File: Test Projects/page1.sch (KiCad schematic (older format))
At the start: 21 parts, among them P1 CONN_01X02, U1 LDO-adj-4term, U2 LDO-adj-4term, U3 Teensy_3.2, U4 LDO-adj-4term

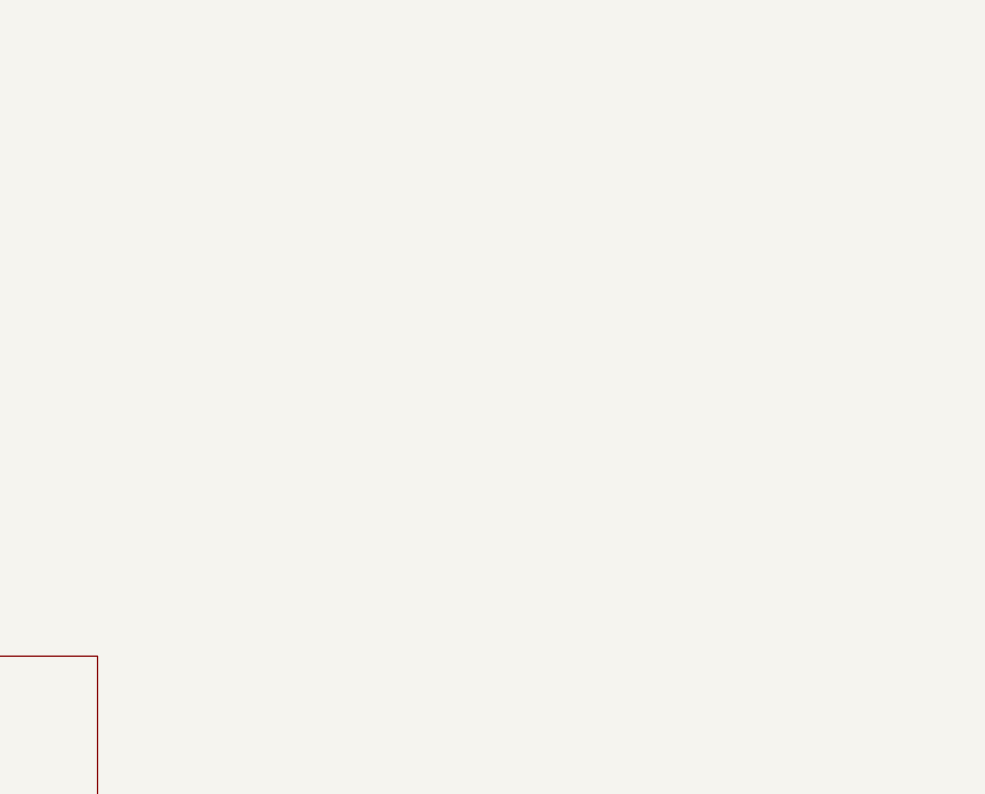
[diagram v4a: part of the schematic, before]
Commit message: Added holes, moved layout
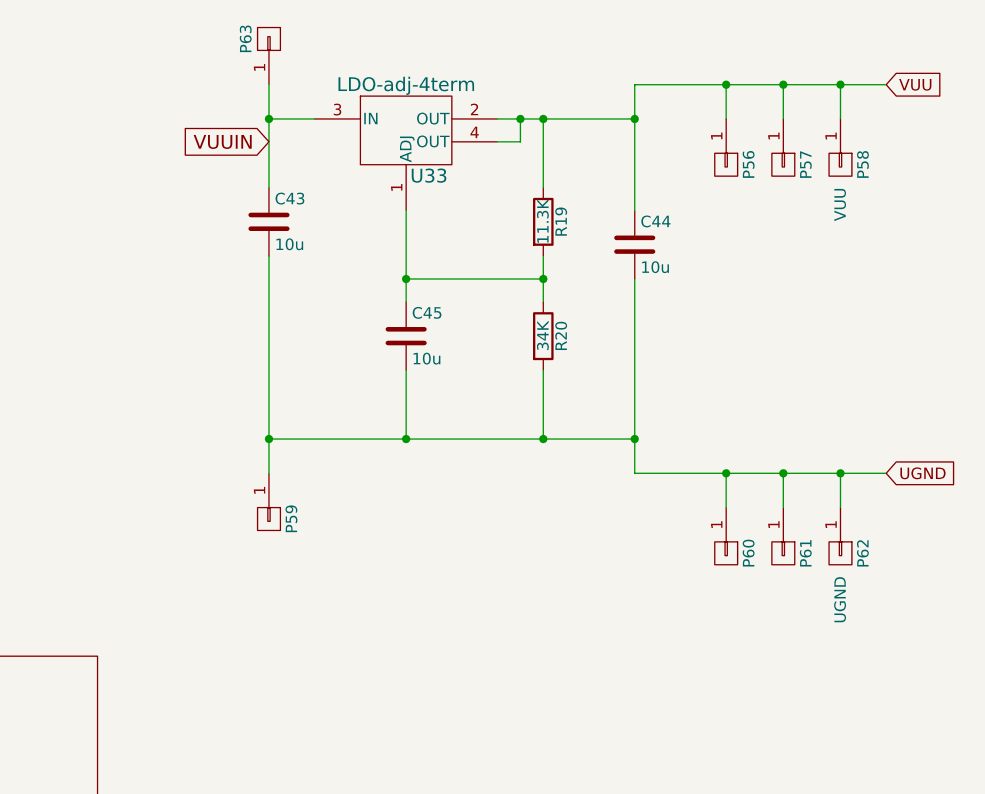
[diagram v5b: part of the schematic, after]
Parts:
- added C43, C44, C45: 10u, Capacitors_Tantalum_SMD:TantalC_SizeB_EIA-3528_Reflow, symbol C
- added P56, P57, P59, P60, P61: CONN_01X01, SparkFun-Footprints:TestHole, symbol CONN_01X01
- added P58: VUU, Pin_Headers:Pin_Header_Straight_1x01, symbol CONN_01X01
- added P62: UGND, Pin_Headers:Pin_Header_Straight_1x01, symbol CONN_01X01
- added P63: CONN_01X01, Pin_Headers:Pin_Header_Straight_1x01, symbol CONN_01X01
- added R19: 11.3K, Resistors_SMD:R_0603, symbol R
- added R20: 34K, Resistors_SMD:R_0603, symbol R
- added U33: LDO-adj-4term, SparkFun-Footprints:SF-SOT-223, symbol LDO-adj-4term
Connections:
- new net: C45.1, R19.2, R20.1, U33.1 (ADJ)
- new net UGND: C43.2, C44.2, C45.2, P59.1 (P1), P60.1 (P1), P61.1 (P1), P62.1 (P1), R20.2
- new net VUU: C44.1, P56.1 (P1), P57.1 (P1), P58.1 (P1), R19.1, U33.2 (OUT), U33.4 (OUT)
- new net VUUIN: C43.1, P63.1 (P1), U33.3 (IN)
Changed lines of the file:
@@
 	3300 3350 3300 3250
 Connection ~ 3300 3250
-Wire Wire Line
-	1950 1650 1950 3250
 Connection ~ 1950 3250
 $Comp
@@
 Text GLabel 4850 4350 0    50   UnSpc ~ 0
 +3V3_TOUT
+$Comp
+L R R20
+U 1 1 56A39733
+P 8200 2700
+F 0 "R20" V 8280 2700 50  0000 C CNN
+F 1 "34K" V 8200 2700 50  0000 C CNN
+F 2 "Resistors_SMD:R_0603" V 8130 2700 50  0001 C CNN
+F 3 "" H 8200 2700 50  0000 C CNN
+	1    8200 2700
+	1    0    0    -1
+$EndComp
+$Comp
+L R R19
+U 1 1 56A39739
+P 8200 2200
+F 0 "R19" V 8280 2200 50  0000 C CNN
+F 1 "11.3K" V 8200 2200 50  0000 C CNN
+F 2 "Resistors_SMD:R_0603" V 8130 2200 50  0001 C CNN
+F 3 "" H 8200 2200 50  0000 C CNN
+	1    8200 2200
+	1    0    0    -1
+$EndComp
+Wire Wire Line
+	8000 1750 8600 1750
+Wire Wire Line
+	8600 1600 8600 2150
+Wire Wire Line
+	8200 1750 8200 2050
+Wire Wire Line
+	8200 2350 8200 2550
+Wire Wire Line
+	8200 2450 7600 2450
+Wire Wire Line
+	7600 2150 7600 2550
+Connection ~ 8200 2450
+Connection ~ 8200 1750
+Wire Wire Line
+	8200 3150 8200 2850
+$Comp
+L C C44
+U 1 1 56A3974E
+P 8600 2300
+F 0 "C44" H 8625 2400 50  0000 L CNN
+F 1 "10u" H 8625 2200 50  0000 L CNN
+F 2 "Capacitors_Tantalum_SMD:TantalC_SizeB_EIA-3528_Reflow" H 8638 2150 50  0001 C CNN
+F 3 "" H 8600 2300 50  0000 C CNN
+	1    8600 2300
+	1    0    0    -1
+$EndComp
+$Comp
+L C C45
+U 1 1 56A39754
+P 7600 2700
+F 0 "C45" H 7625 2800 50  0000 L CNN
+F 1 "10u" H 7625 2600 50  0000 L CNN
+F 2 "Capacitors_Tantalum_SMD:TantalC_SizeB_EIA-3528_Reflow" H 7638 2550 50  0001 C CNN
+F 3 "" H 7600 2700 50  0000 C CNN
+	1    7600 2700
+	1    0    0    -1
+$EndComp
+Wire Wire Line
+	8600 2450 8600 3300
+Connection ~ 8600 1750
+Connection ~ 7600 2450
+Wire Wire Line
+	7600 2850 7600 3150
+Wire Wire Line
+	7000 1750 7200 1750
+$Comp
+L C C43
+U 1 1 56A3976B
+P 7000 2200
+F 0 "C43" H 7025 2300 50  0000 L CNN
+F 1 "10u" H 7025 2100 50  0000 L CNN
+F 2 "Capacitors_Tantalum_SMD:TantalC_SizeB_EIA-3528_Reflow" H 7038 2050 50  0001 C CNN
+F 3 "" H 7000 2200 50  0000 C CNN
+	1    7000 2200
+	1    0    0    -1
+$EndComp
+Wire Wire Line
+	7000 1600 7000 2050
+Connection ~ 7000 1750
+Wire Wire Line
+	7000 2350 7000 3300
+$Comp
+L LDO-adj-4term U33
+U 1 1 56A3977A
+P 7600 1750
+F 0 "U33" H 7700 1500 60  0000 C CNN
+F 1 "LDO-adj-4term" H 7600 1900 60  0000 C CNN
+F 2 "SparkFun-Footprints:SF-SOT-223" H 7600 1750 60  0001 C CNN
+F 3 "" H 7600 1750 60  0000 C CNN
+	1    7600 1750
+	1    0    0    -1
+$EndComp
+Wire Wire Line
+	8000 1850 8100 1850
+Wire Wire Line
+	8100 1850 8100 1750
+Connection ~ 8100 1750
+Wire Wire Line
+	7000 3150 8600 3150
+Connection ~ 7600 3150
+Connection ~ 8200 3150
+Wire Wire Line
+	8600 3300 9700 3300
+Connection ~ 8600 3150
+Wire Wire Line
+	8600 1600 9700 1600
+Text GLabel 9700 1600 2    50   Input ~ 0
+VUU
+Text GLabel 9700 3300 2    50   Input ~ 0
+UGND
+$Comp
+L CONN_01X01 P56
+U 1 1 56A3A761
+P 9000 1950
+F 0 "P56" H 9000 2050 50  0000 C CNN
+F 1 "CONN_01X01" H 9100 1950 50  0001 L CNN
+F 2 "SparkFun-Footprints:TestHole" H 9000 1950 50  0001 C CNN
+F 3 "" H 9000 1950 50  0000 C CNN
+	1    9000 1950
+	0    1    1    0
+$EndComp
+$Comp
+L CONN_01X01 P57
+U 1 1 56A3AA28
+P 9250 1950
+F 0 "P57" H 9250 2050 50  0000 C CNN
+F 1 "CONN_01X01" H 9350 1950 50  0001 L CNN
+F 2 "SparkFun-Footprints:TestHole" H 9250 1950 50  0001 C CNN
+F 3 "" H 9250 1950 50  0000 C CNN
+	1    9250 1950
+	0    1    1    0
+$EndComp
+$Comp
+L CONN_01X01 P58
+U 1 1 56A3AAB7
+P 9500 1950
+F 0 "P58" H 9500 2050 50  0000 C CNN
+F 1 "VUU" H 9600 1950 50  0000 L CNN
+F 2 "Pin_Headers:Pin_Header_Straight_1x01" H 9500 1950 50  0001 C CNN
+F 3 "" H 9500 1950 50  0000 C CNN
+	1    9500 1950
+	0    1    1    0
+$EndComp
+Wire Wire Line
+	9000 1750 9000 1600
+Connection ~ 9000 1600
+Wire Wire Line
+	9250 1750 9250 1600
+Connection ~ 9250 1600
+Wire Wire Line
+	9500 1750 9500 1600
+Connection ~ 9500 1600
+$Comp
+L CONN_01X01 P60
+U 1 1 56A3B3A0
+P 9000 3650
+F 0 "P60" H 9000 3750 50  0000 C CNN
+F 1 "CONN_01X01" H 9100 3650 50  0001 L CNN
+F 2 "SparkFun-Footprints:TestHole" H 9000 3650 50  0001 C CNN
+F 3 "" H 9000 3650 50  0000 C CNN
+	1    9000 3650
+	0    1    1    0
+$EndComp
+$Comp
+L CONN_01X01 P61
+U 1 1 56A3B3A6
+P 9250 3650
+F 0 "P61" H 9250 3750 50  0000 C CNN
+F 1 "CONN_01X01" H 9350 3650 50  0001 L CNN
+F 2 "SparkFun-Footprints:TestHole" H 9250 3650 50  0001 C CNN
+F 3 "" H 9250 3650 50  0000 C CNN
+	1    9250 3650
+	0    1    1    0
+$EndComp
+$Comp
+L CONN_01X01 P62
+U 1 1 56A3B3AC
+P 9500 3650
+F 0 "P62" H 9500 3750 50  0000 C CNN
+F 1 "UGND" H 9600 3650 50  0000 L CNN
+F 2 "Pin_Headers:Pin_Header_Straight_1x01" H 9500 3650 50  0001 C CNN
+F 3 "" H 9500 3650 50  0000 C CNN
+	1    9500 3650
+	0    1    1    0
+$EndComp
+Wire Wire Line
+	9000 3450 9000 3300
+Wire Wire Line
+	9250 3450 9250 3300
+Wire Wire Line
+	9500 3450 9500 3300
+Connection ~ 9000 3300
+Connection ~ 9250 3300
+Connection ~ 9500 3300
+Connection ~ 7000 3150
+$Comp
+L CONN_01X01 P59
+U 1 1 56A3B4F3
+P 7000 3500
+F 0 "P59" H 7000 3600 50  0000 C CNN
+F 1 "CONN_01X01" H 7100 3500 50  0001 L CNN
+F 2 "SparkFun-Footprints:TestHole" H 7000 3500 50  0001 C CNN
+F 3 "" H 7000 3500 50  0000 C CNN
+	1    7000 3500
+	0    1    1    0
+$EndComp
+Wire Wire Line
+	1950 1650 1950 3250
+$Comp
+L CONN_01X01 P63
+U 1 1 56A3C8A9
+P 7000 1400
+F 0 "P63" H 7000 1500 50  0000 C CNN
+F 1 "CONN_01X01" H 7100 1400 50  0001 L CNN
+F 2 "Pin_Headers:Pin_Header_Straight_1x01" H 7000 1400 50  0001 C CNN
+F 3 "" H 7000 1400 50  0000 C CNN
+	1    7000 1400
+	0    -1   -1   0
+$EndComp
+Text GLabel 7000 1850 0    60   Input ~ 0
+VUUIN
 $EndSCHEMATC

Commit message: Routing, 15%
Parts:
- added JACK12: POWER_JACKPTH, SparkFun-Footprints:SparkFun-Connectors-POWER_JACK_PTH, symbol POWER_JACKPTH
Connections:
- net GND: now also JACK12.GND
- net Bulk_IN renamed VBULK
- net VBULK: now also JACK12.PWR
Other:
- moved on the sheet: C1, C2, C3, C4, C43, C44, C45, C5, C6, C7, C8, C9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
